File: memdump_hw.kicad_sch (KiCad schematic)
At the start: 76 parts, among them IC1 4094D, IC2 4094D, IC3 4094D, J1 USB_C_USB2.0, J2 SWD, J3 LEVEL, J4 BOOT0, Q1 SI4800, SW1 RESET, U1 AMS1117-3.3, U2 STM32F103C8Tx, U6 SST39SF040, Y1 12M

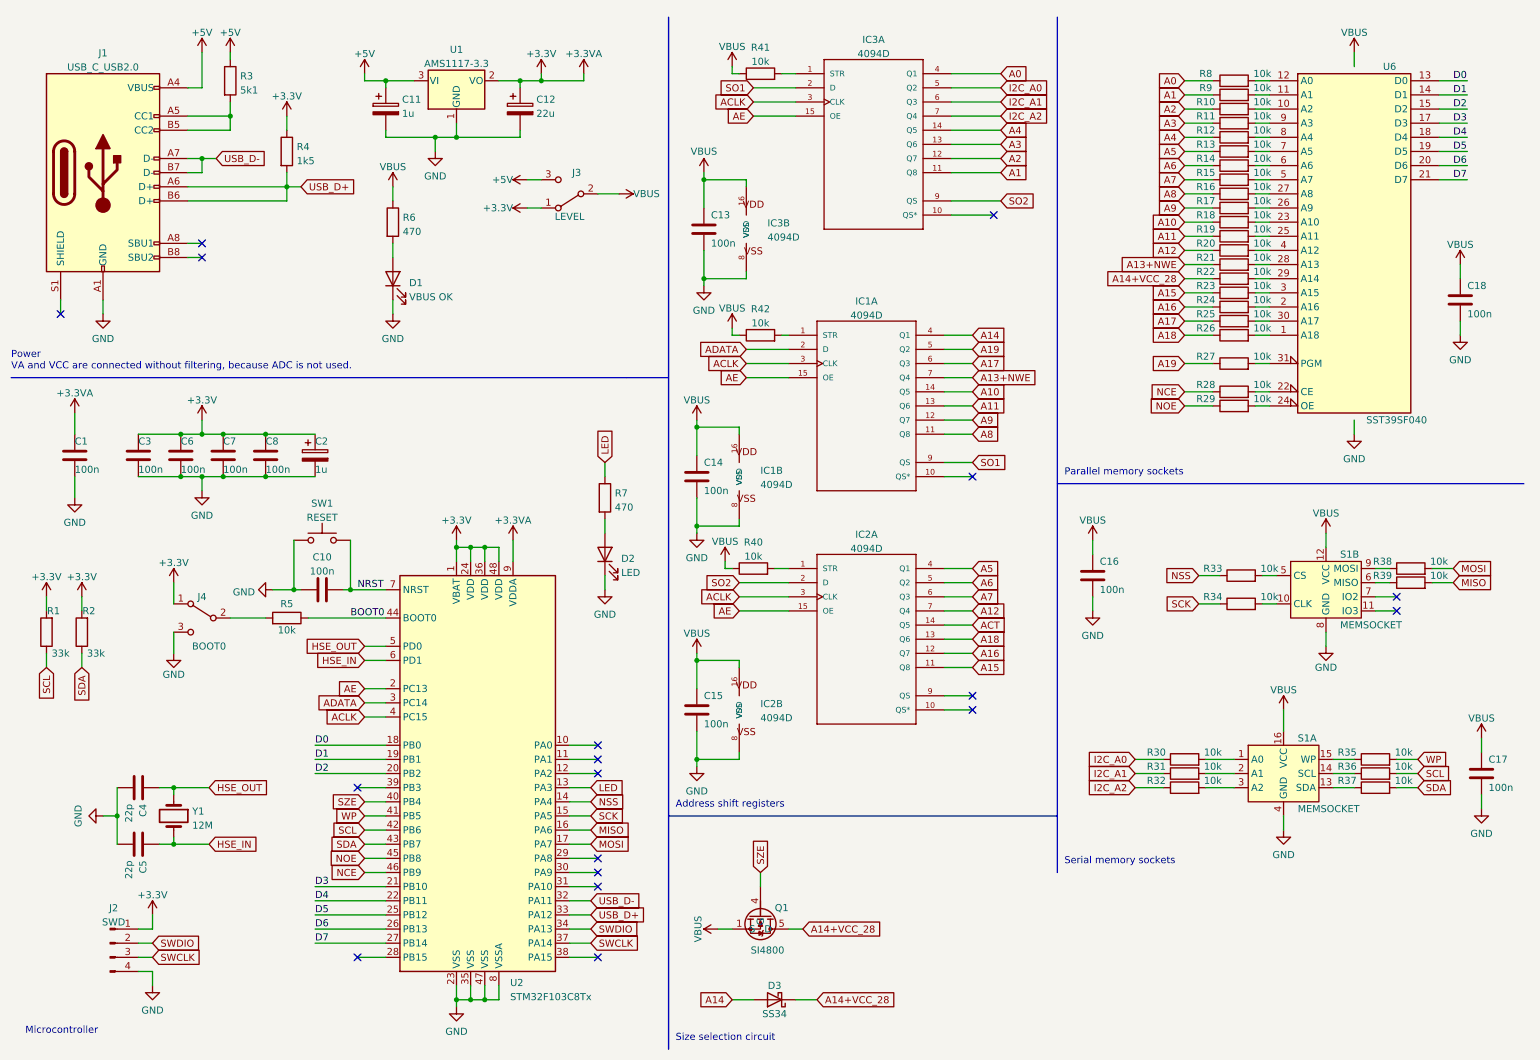
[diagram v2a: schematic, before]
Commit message: fix: change to 74HC595 fix: all tracks are routed fix: GND is now continuous fix: everything else, the board is pretty much complete
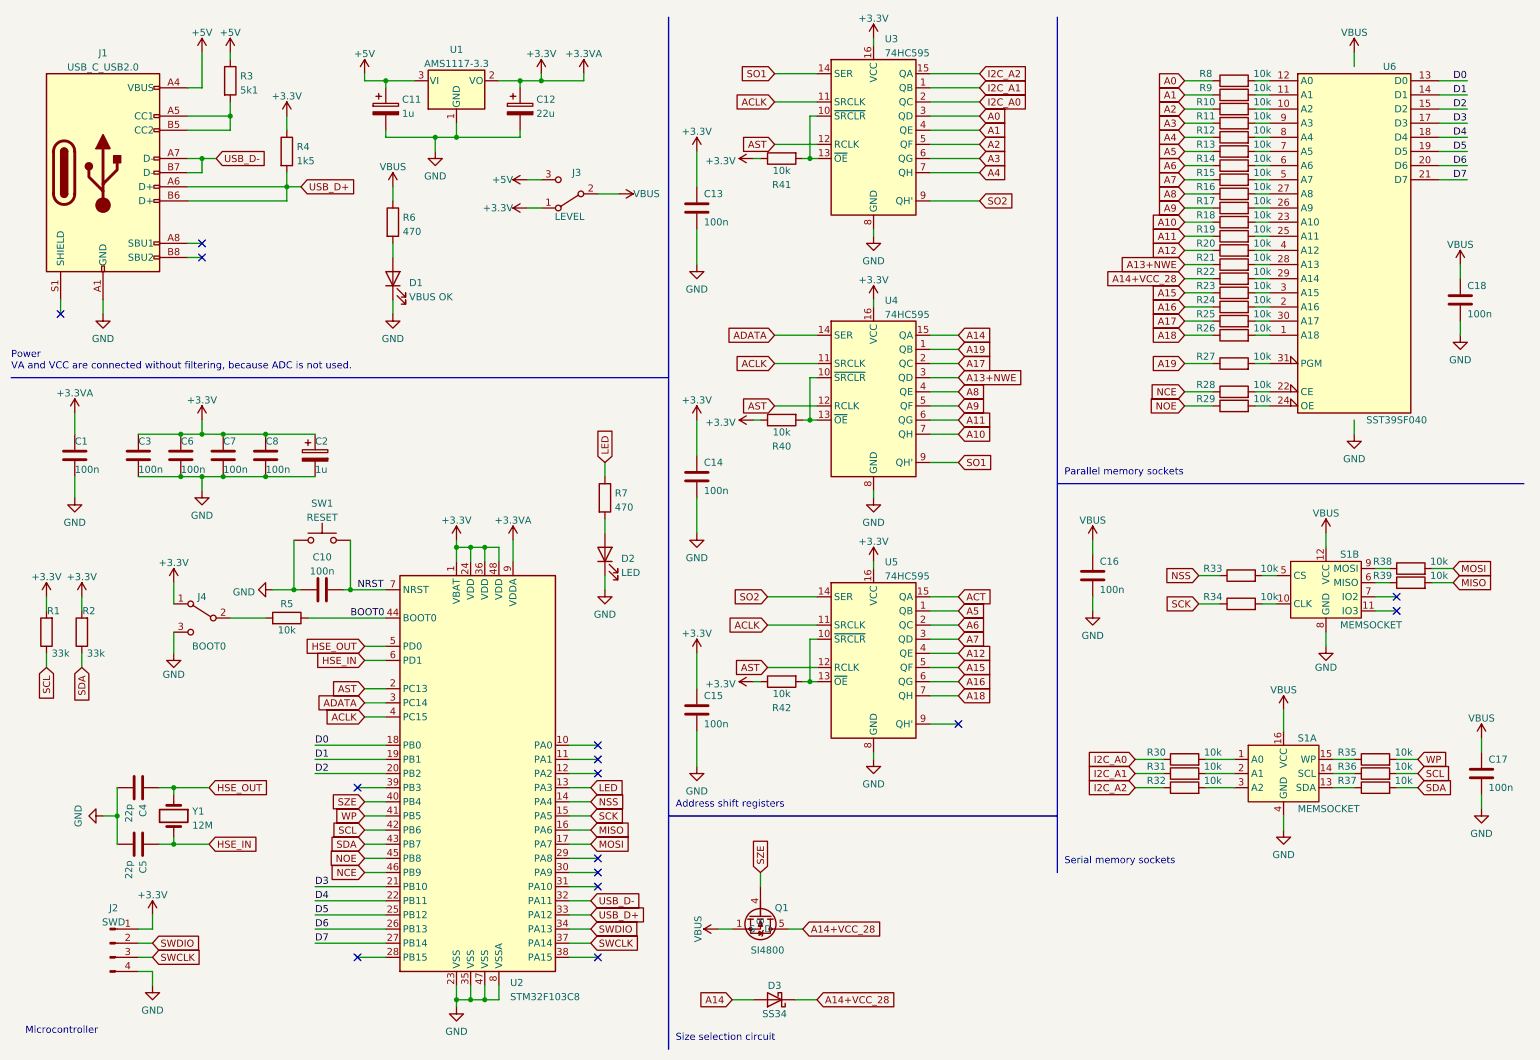
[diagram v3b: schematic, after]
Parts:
- removed IC1, IC2, IC3: 4094D, Package_SO:SOIC-16_3.9x9.9mm_P1.27mm, symbol 40xx:4094D
- added U3, U4, U5: 74HC595, Package_SO:SOP-16_3.9x9.9mm_P1.27mm, symbol 74xx:74HC595
- U2: value STM32F103C8Tx -> STM32F103C8
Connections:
- net +3.3VA: now also C13.1, C14.1, C15.1, R40.1, R41.1, R42.1, U3.16 (VCC), U4.16 (VCC), U5.16 (VCC)
- net A0: now also U3.3 (QD)
- net A1: now also U3.4 (QE)
- net A10: now also U4.7 (QH)
- net A11: now also U4.6 (QG)
- net A12: now also U5.4 (QE)
- net A13+NWE: now also U4.3 (QD)
- net A14: now also U4.15 (QA)
- net A15: now also U5.5 (QF)
- net A16: now also U5.6 (QG)
- net A17: now also U4.2 (QC)
- net A18: now also U5.7 (QH)
- net A19: now also U4.1 (QB)
- net A2: now also U3.5 (QF)
- net A3: now also U3.6 (QG)
- net A4: now also U3.7 (QH)
- net A5: now also U5.1 (QB)
- net A6: now also U5.2 (QC)
- net A7: now also U5.3 (QD)
- net A8: now also U4.4 (QE)
- net A9: now also U4.5 (QF)
- net ACLK: now also U3.11 (SRCLK), U4.11 (SRCLK), U5.11 (SRCLK)
- net ACT: now also U5.15 (QA)
- net ADATA: now also U4.14 (SER)
- net GND: now also U3.8 (GND), U4.8 (GND), U5.8 (GND)
- net I2C_A0: now also U3.2 (QC)
- net I2C_A1: now also U3.1 (QB)
- net I2C_A2: now also U3.15 (QA)
- net SO1: now also U3.14 (SER), U4.9 (QH')
- net SO2: now also U3.9 (QH'), U5.14 (SER)
- net VBUS: no longer C13.1, C14.1, C15.1, R40.1, R41.1, R42.1
- net at R41.2: now also U3.10 (~{SRCLR}), U3.13 (~{OE})
- net at R42.2: now also U5.10 (~{SRCLR}), U5.13 (~{OE})
- net at R40.2: now also U4.10 (~{SRCLR}), U4.13 (~{OE})
- net AE renamed AST
- net AST: now also U3.12 (RCLK), U4.12 (RCLK), U5.12 (RCLK)
- no-connect marks 18 -> 15
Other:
- moved on the sheet: C13, R41

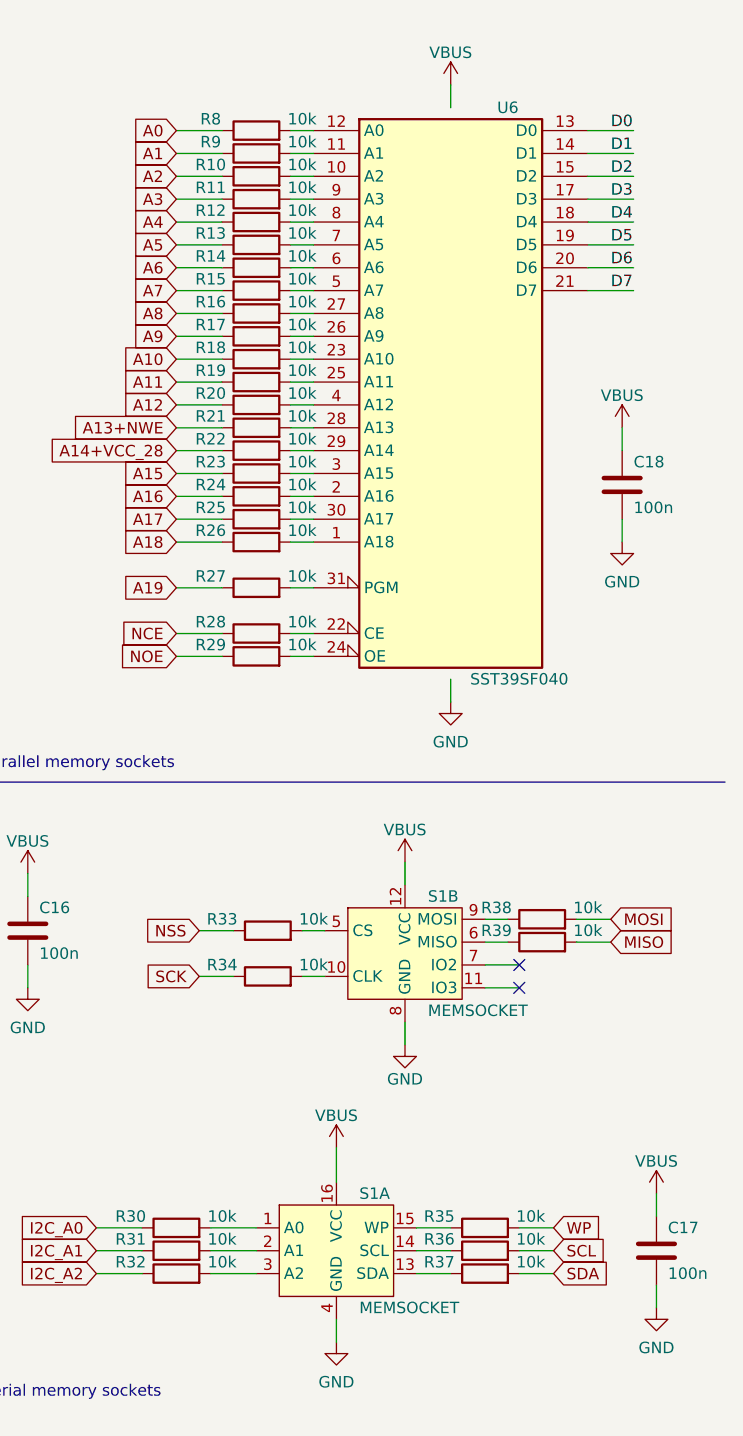
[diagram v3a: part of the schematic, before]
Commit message: fix: changed protection resistances to 470R for faster operation
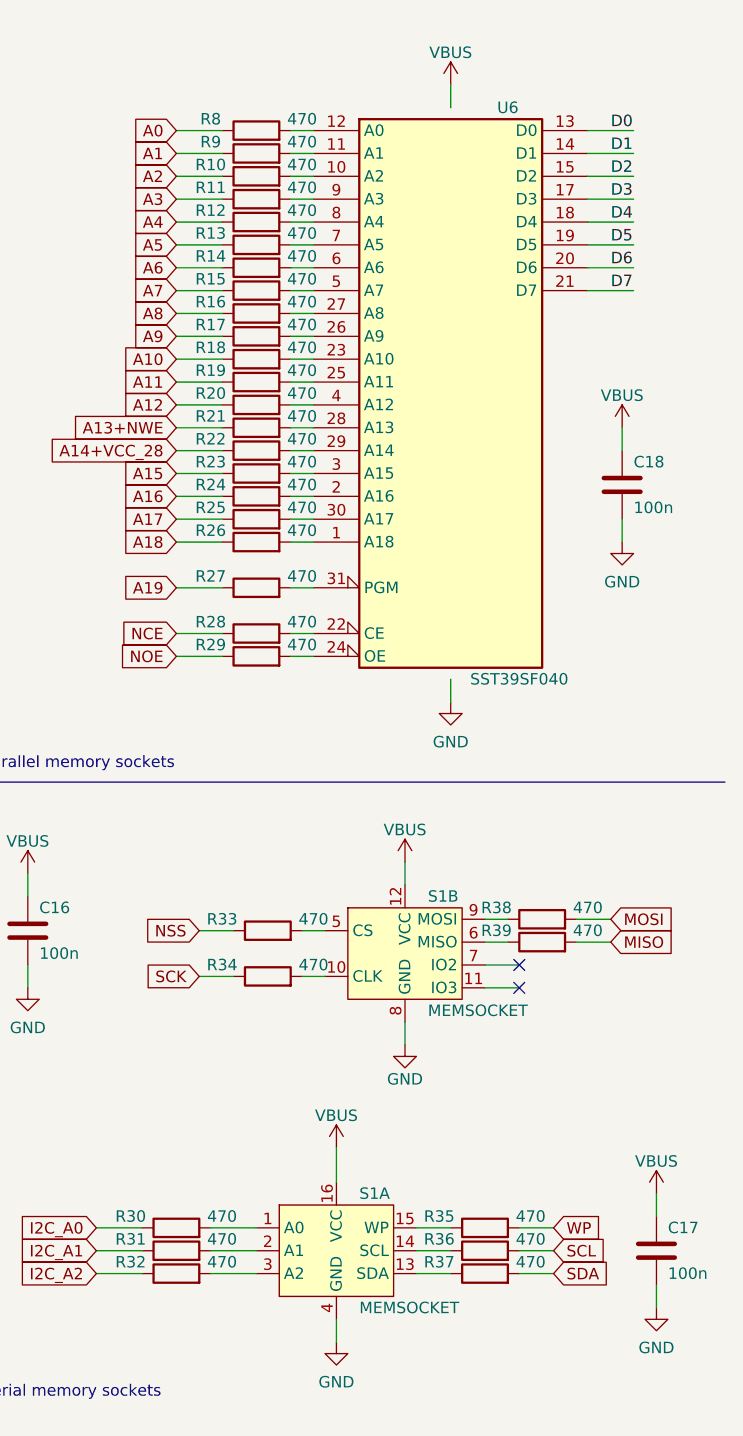
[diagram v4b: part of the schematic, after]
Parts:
- R10, R11, R12, R13, R14, R15, R16, R17, R18, R19, R20, R21, R22, R23, R24, R25, R26, R27, R28, R29, R30, R31, R32, R33, R34, R35, R36, R37, R38, R39, R8, R9: value 10k -> 470
